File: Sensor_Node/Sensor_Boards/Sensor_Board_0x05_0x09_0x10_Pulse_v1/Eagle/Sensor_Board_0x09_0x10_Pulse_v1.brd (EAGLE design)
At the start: 55 x 35 mm, 20 parts, among them J3 1x3 RA Female .1", J4 ARDUINO_ISP, J6 1x3 RA Female .1", U2 ATMEGA328P_TQFP, Y1 8MHZ

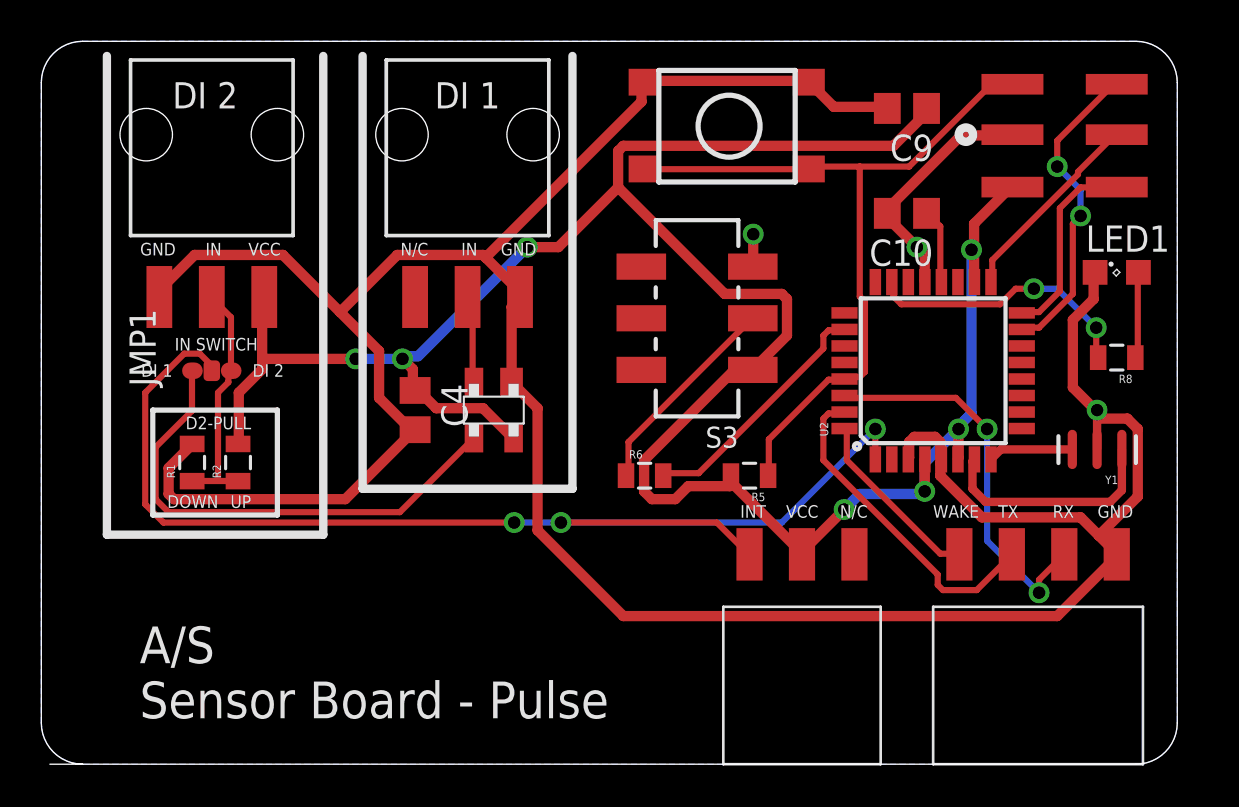
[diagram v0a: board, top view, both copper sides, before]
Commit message: Changes on SensModule Pulse
- moved connectors closer together
- turned various components
- added pogopin programming connector
- removed digital input jumper and put digi_input 1 and 2 directly to
PD2, PD3
- put wakeup on PC1
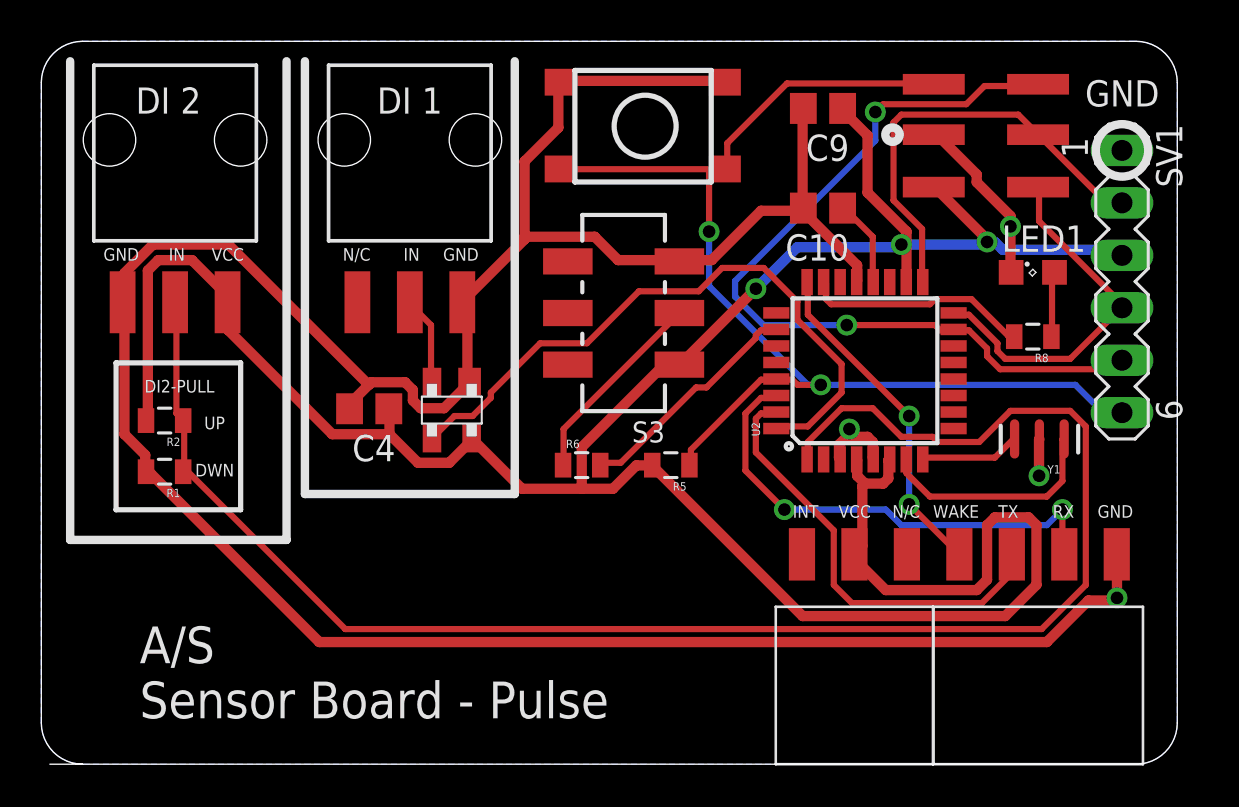
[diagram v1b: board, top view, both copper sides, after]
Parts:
- removed JMP1: 0R-JUMPC, jump-0r-smd:C0R-JMP
- added SV1: (no value), con-lstb:MA06-1
- moved R8 4.19 mm to (48.0, 20.7)
- moved R2 4.10 mm to (5.97, 16.6), turned to 180 degrees
- moved C10 4.07 mm to (37.8, 26.9)
- moved C9 4.06 mm to (37.8, 31.8)
- moved LED1 4.06 mm to (48.0, 23.8)
- moved S1 4.06 mm to (25.1, 33.0)
- moved R5 3.84 mm to (30.5, 14.5)
- moved J4 3.81 mm to (48.3, 27.9)
- moved S3 3.57 mm to (28.2, 21.8)
- moved U2 3.30 mm to (39.9, 19.1)
- moved R6 3.09 mm to (26.2, 14.5)
- moved Y1 2.84 mm to (48.3, 15.7)
- moved J6 2.81 mm to (17.8, 29.6)
- moved U$15 2.54 mm to (36.8, 10.2)
- moved C4 2.22 mm to (15.9, 17.2), turned to 180 degrees
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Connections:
- net DIGITAL_INPUT_1: now also U2.32; no longer JMP1.1
- net DIGITAL_INPUT_2: now also U2.1; no longer JMP1.3
- net GND: now also SV1.1
- net INT_INPUT: no longer JMP1.2, U2.1
- net MISO: now also SV1.4
- net MOSI: now also SV1.5
- net RESET: now also SV1.6
- net SCK: now also SV1.2
- net VCC: now also SV1.3
- net WAKE_UP: now also U2.24; no longer U2.32
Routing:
- net DIGITAL_INPUT_2: track 11.8 -> 80.5 mm
- net INT_INPUT: track 58.7 -> 0.00 mm, vias 3 -> 0
- net MOSI: track 15.3 -> 40.8 mm
- net RESET: track 37.3 -> 57.9 mm, vias 0 -> 2
- net VCC: track 115.5 -> 131.7 mm, vias 7 -> 3
- net SCK: track 9.70 -> 21.3 mm
- net MISO: track 9.47 -> 18.0 mm
- net GND: track 158.3 -> 149.9 mm, vias 3 -> 4
- net WAKE_UP: track 8.96 -> 16.2 mm, vias 0 -> 2
- net DIGITAL_INPUT_1: track 24.1 -> 31.1 mm
- net MCU_TXO: track 15.9 -> 21.2 mm
- net MCU_RXI: track 18.9 -> 23.6 mm
- net L1: track 13.3 -> 11.0 mm, vias 2 -> 0
- net N$30: track 4.21 -> 3.21 mm
- net DBG_ENABLE: track 12.1 -> 11.3 mm
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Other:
- board text added: "DI2-PULL"
- board text added: "DWN"
- board text removed: "D2-PULL"
- board text removed: "DOWN"
- board text removed: "IN SWITCH"

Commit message: Changes on all boards
- added capacitor on reset-path
- changed order of pogopin programmer pins

Pulse-Board:
- Deleted input-jumper. Currently one interrupt-pin missing, so print is
not yet routed.
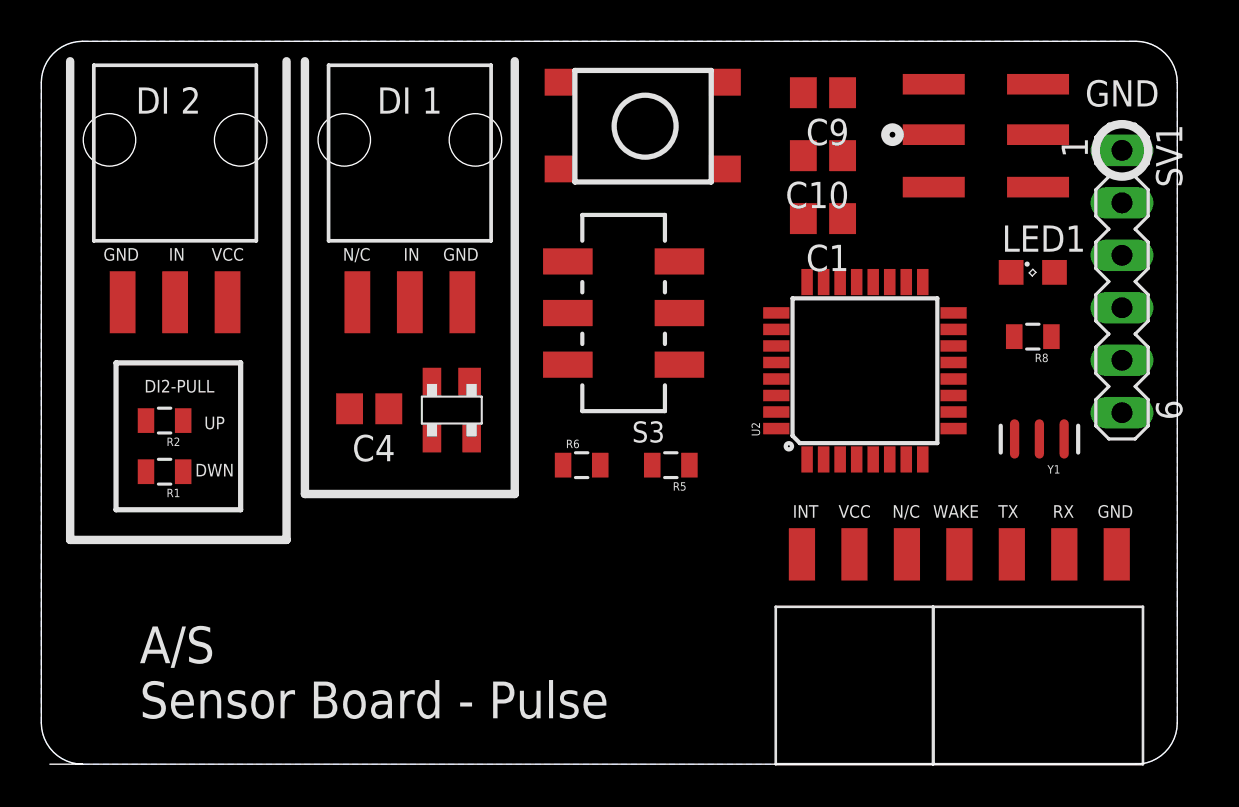
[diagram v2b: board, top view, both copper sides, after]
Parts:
- added C1: 100n, eagle-ltspice:C0805
- moved C10 2.54 mm to (37.8, 29.5)
- moved C9 0.76 mm to (37.8, 32.5)
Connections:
- new net N$5: C1.2, R5.1, S1.3, S1.4, U2.29
- net MISO: now also SV1.6; no longer SV1.4
- net MOSI: now also SV1.2; no longer SV1.5
- net RESET: now also C1.1, SV1.4; no longer R5.1, S1.3, S1.4, SV1.6, U2.29
- net SCK: now also SV1.5; no longer SV1.2
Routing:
- net GND: track 149.9 -> 0.00 mm, vias 4 -> 0
- net VCC: track 131.7 -> 0.00 mm, vias 3 -> 0
- net DIGITAL_INPUT_2: track 80.5 -> 0.00 mm
- net RESET: track 57.9 -> 0.00 mm, vias 2 -> 0
- net MOSI: track 40.8 -> 0.00 mm, vias 2 -> 0
- net DIGITAL_INPUT_1: track 31.1 -> 0.00 mm
- net MCU_RXI: track 23.6 -> 0.00 mm, vias 2 -> 0
- net SCK: track 21.3 -> 0.00 mm
- net MCU_TXO: track 21.2 -> 0.00 mm
- net MISO: track 18.0 -> 0.00 mm
- net WAKE_UP: track 16.2 -> 0.00 mm, vias 2 -> 0
- net DBG_ENABLE: track 11.3 -> 0.00 mm
- net N$2: track 11.1 -> 0.00 mm
- net L1: track 11.0 -> 0.00 mm
- net N$3: track 9.69 -> 0.00 mm
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
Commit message: Changed some SensorBoards
SHT31
- new routing

PULSE
- pogopin programmer now over FTDI
- interrupt to comboard now comes from atmega

TSL2561
- pogopin programmer now over FTDI

PROTOYPING
- changed title of schematic
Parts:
- moved U$15 2.54 mm to (34.3, 10.2)
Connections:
- removed net INT_INPUT: U$15.1
- new net FTDI_RXI: SV1.4, U2.30
- new net FTDI_TXO: SV1.5, U2.31
- new net INT_TO_COM: U$15.1, U2.2
- net GND: now also SV1.2
- net MCU_RXI: now also U2.11; no longer U2.30
- net MCU_TXO: now also U2.10; no longer U2.31
- net MISO: no longer SV1.6
- net MOSI: no longer SV1.2
- net RESET: now also SV1.6; no longer SV1.4
- net SCK: no longer SV1.5
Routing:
- net GND: track 0.00 -> 99.7 mm, vias 0 -> 6
- net VCC: track 0.00 -> 89.1 mm, vias 0 -> 2
- net DIGITAL_INPUT_2: track 0.00 -> 44.5 mm, vias 0 -> 2
- net RESET: track 0.00 -> 35.3 mm, vias 0 -> 3
- net N$5: track 0.00 -> 28.2 mm, vias 0 -> 2
- net DIGITAL_INPUT_1: track 0.00 -> 20.6 mm, vias 0 -> 2
- net FTDI_RXI: track 0.00 -> 20.0 mm, vias 0 -> 1
- net FTDI_TXO: track 0.00 -> 17.8 mm, vias 0 -> 1
- net DBG_ENABLE: track 0.00 -> 17.5 mm, vias 0 -> 2
- net MOSI: track 0.00 -> 16.5 mm, vias 0 -> 2
- net WAKE_UP: track 0.00 -> 16.4 mm, vias 0 -> 2
- net MCU_TXO: track 0.00 -> 14.0 mm
- net MCU_RXI: track 0.00 -> 13.9 mm, vias 0 -> 2
- net SCK: track 0.00 -> 13.1 mm, vias 0 -> 2
- net L1: track 0.00 -> 12.1 mm, vias 0 -> 2
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
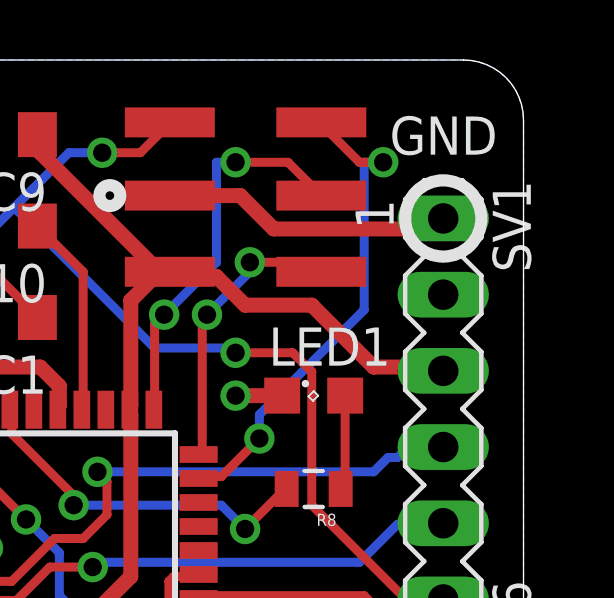
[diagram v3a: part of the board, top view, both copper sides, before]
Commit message: Finished some boards.
- Minor changes on all boards except
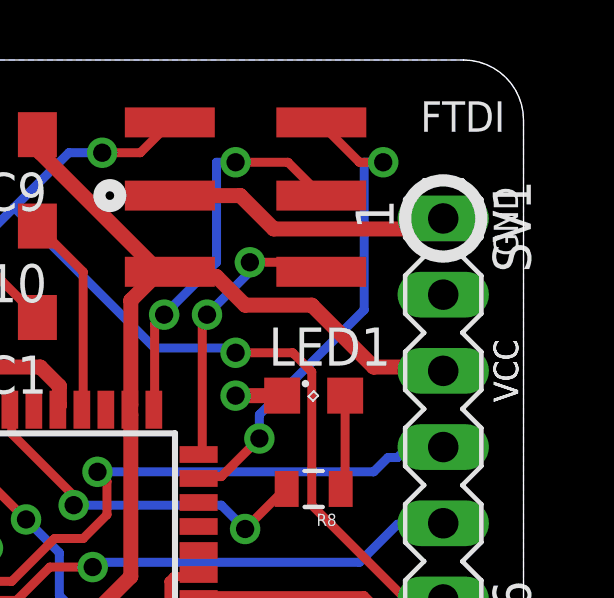
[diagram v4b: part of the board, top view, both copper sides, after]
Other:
- board text added: "FTDI"
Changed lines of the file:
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@@
 <setting verticaltext="up"/>
 </settings>
-<grid distance="0.1" unitdist="inch" unit="inch" style="lines" multiple="1" display="yes" altdistance="0.5" altunitdist="mm" altunit="mm"/>
+<grid distance="0.01" unitdist="inch" unit="inch" style="lines" multiple="1" display="yes" altdistance="0.5" altunitdist="mm" altunit="mm"/>
 <layers>
 <layer number="1" name="Top" color="4" fill="1" visible="yes" active="yes"/>
@@
 <hole x="14.6685" y="30.226" drill="2.54"/>
 <circle x="41.2115" y="30.48" radius="0.3474125" width="0.4064" layer="21"/>
-<text x="54.13375" y="33.11525" size="1.27" layer="21" rot="R180">GND</text>
+<text x="54.38775" y="33.62325" size="1.016" layer="21" rot="R180">FTDI</text>
 <circle x="52.324" y="29.718" radius="1.27" width="0.4064" layer="21"/>
+<text x="54.00675" y="30.76575" size="0.8128" layer="21" rot="R270">GND</text>
+<text x="54.00675" y="25.68575" size="0.8128" layer="21" rot="R270">VCC</text>
+<text x="54.00675" y="25.68575" size="0.8128" layer="21" rot="R270">VCC</text>
 </plain>
 <attributes>

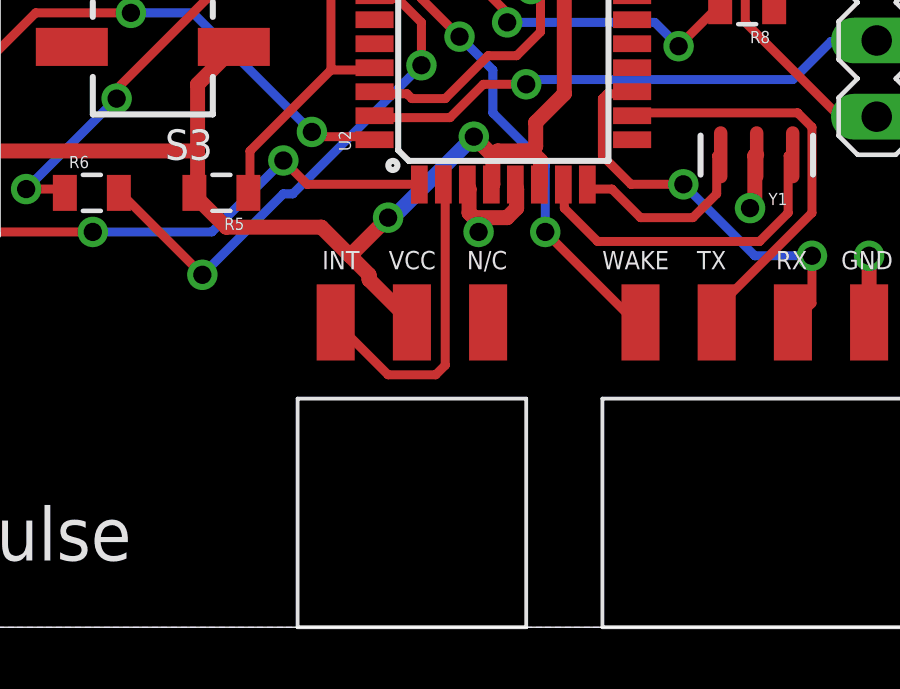
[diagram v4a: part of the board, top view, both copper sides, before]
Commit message: Removed gap between connector to commBoard
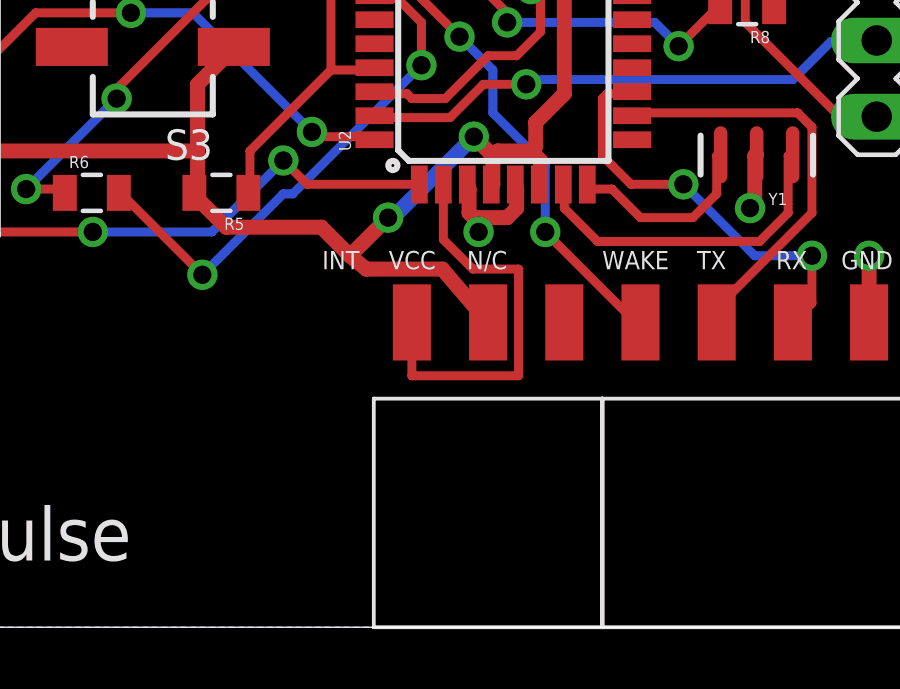
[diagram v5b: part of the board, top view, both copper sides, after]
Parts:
- moved U$15 2.54 mm to (36.8, 10.2)
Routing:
- net INT_TO_COM: track 10.5 -> 13.6 mm
- net VCC: track 89.1 -> 91.6 mm
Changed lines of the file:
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@@
 <?xml version="1.0" encoding="utf-8"?>
 <!DOCTYPE eagle SYSTEM "eagle.dtd">
-<eagle version="8.1.1">
+<eagle version="8.2.2">
 <drawing>
 <settings>
@@
 <element name="R1" library="SparkFun-Passives" package="0805" value="10k" x="5.969" y="14.1605" rot="R180"/>
 <element name="R2" library="SparkFun-Passives" package="0805" value="10k" x="5.969" y="16.637" rot="R180"/>
-<element name="U$15" library="myownthings" package="M03_SMD_90" value="M03_SMD_90" x="34.29" y="10.16"/>
+<element name="U$15" library="myownthings" package="M03_SMD_90" value="M03_SMD_90" x="36.83" y="10.16"/>
 <element name="U$16" library="myownthings" package="M04_SMD_90" value="M04_SMD_90" x="44.45" y="10.16"/>
 <element name="SV1" library="con-lstb" package="MA06-1" value="" x="52.324" y="23.368" rot="R270">
@@
 <wire x1="16.8275" y1="17.145" x2="16.825" y2="17.2085" width="0.5" layer="1"/>
 <wire x1="20.6375" y1="15.71625" x2="20.8355" y2="15.795" width="0.5" layer="1"/>
-<wire x1="35.40125" y1="11.58875" x2="36.83" y2="10.16" width="0.5" layer="1"/>
-<wire x1="35.40125" y1="11.7475" x2="35.40125" y2="11.58875" width="0.5" layer="1"/>
+<wire x1="37.846" y1="11.938" x2="39.37" y2="10.16" width="0.5" layer="1"/>
+<wire x1="35.306" y1="11.938" x2="37.846" y2="11.938" width="0.5" layer="1"/>
 <wire x1="33.81375" y1="13.335" x2="34.76625" y2="12.3825" width="0.5" layer="1"/>
-<wire x1="34.76625" y1="12.3825" x2="35.40125" y2="11.7475" width="0.5" layer="1"/>
+<wire x1="34.76625" y1="12.3825" x2="35.306" y2="11.938" width="0.5" layer="1"/>
 <wire x1="30.63875" y1="13.335" x2="33.81375" y2="13.335" width="0.5" layer="1"/>
 <wire x1="29.68625" y1="14.2875" x2="30.63875" y2="13.335" width="0.5" layer="1"/>
@@
 <contactref element="U$15" pad="1"/>
 <contactref element="U2" pad="2"/>
-<wire x1="37.94125" y1="8.73125" x2="37.94125" y2="14.605" width="0.3" layer="1"/>
-<wire x1="37.62375" y1="8.41375" x2="37.94125" y2="8.73125" width="0.3" layer="1"/>
-<wire x1="36.03625" y1="8.41375" x2="37.62375" y2="8.41375" width="0.3" layer="1"/>
-<wire x1="34.29" y1="10.16" x2="36.03625" y2="8.41375" width="0.3" layer="1"/>
-<wire x1="37.94125" y1="14.605" x2="37.878" y2="14.7574" width="0.3" layer="1"/>
+<wire x1="40.386" y1="11.938" x2="40.386" y2="8.382" width="0.3" layer="1"/>
+<wire x1="36.83" y1="8.382" x2="40.386" y2="8.382" width="0.3" layer="1"/>
+<wire x1="36.83" y1="10.16" x2="36.83" y2="8.382" width="0.3" layer="1"/>
+<wire x1="37.878" y1="14.7574" x2="37.878" y2="12.922" width="0.3" layer="1"/>
+<wire x1="37.878" y1="12.922" x2="38.862" y2="11.938" width="0.3" layer="1"/>
+<wire x1="38.862" y1="11.938" x2="40.386" y2="11.938" width="0.3" layer="1"/>
 </signal>
 <signal name="DIGITAL_INPUT_1">

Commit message: Pulse-Board
- Reset path
- Various small things
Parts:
- moved C9 0.38 mm to (37.8, 32.1)
- moved C10 0.13 mm to (37.8, 29.3)
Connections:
- removed net N$5: C1.2, R5.1, S1.3, S1.4, U2.29
- new net FTDI_RESET: C1.1, SV1.6
- net RESET: now also C1.2, R5.1, S1.3, S1.4, U2.29; no longer C1.1, SV1.6
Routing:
- net VCC: track 91.6 -> 129.3 mm
- net N$5: track 28.2 -> 0.00 mm, vias 2 -> 0
- net FTDI_RESET: track 0.00 -> 19.8 mm
- net N$2: track 11.2 -> 20.2 mm
- net DIGITAL_INPUT_2: track 44.5 -> 53.3 mm
- net INT_TO_COM: track 13.6 -> 5.02 mm
- net GND: track 99.7 -> 92.3 mm, vias 6 -> 8
- net RESET: track 35.3 -> 42.7 mm, vias 3 -> 0
- net L1: track 12.1 -> 19.2 mm
- net MOSI: track 16.5 -> 21.9 mm
- net DIGITAL_INPUT_1: track 20.6 -> 25.9 mm, vias 2 -> 0
- net MCU_TXO: track 14.0 -> 8.94 mm, vias 0 -> 2
- net SCK: track 13.1 -> 9.44 mm
- net DBG_ENABLE: track 17.5 -> 14.8 mm
- net MCU_RXI: track 13.9 -> 11.3 mm
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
